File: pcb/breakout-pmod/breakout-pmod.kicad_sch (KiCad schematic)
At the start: 13 parts, among them J1 FX18-120P-0.8SV20

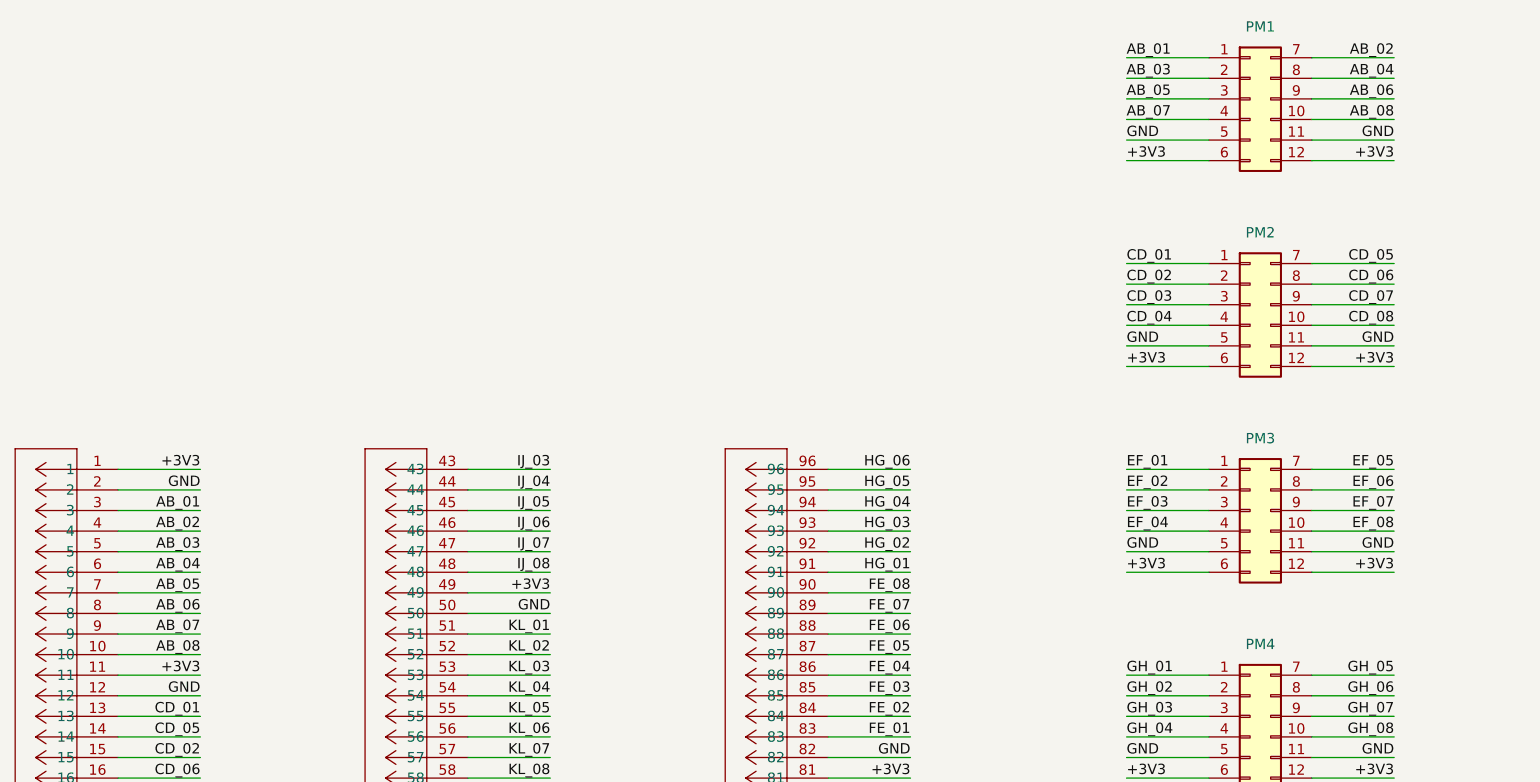
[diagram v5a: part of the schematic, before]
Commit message: [pmod] fix order of AB pmod
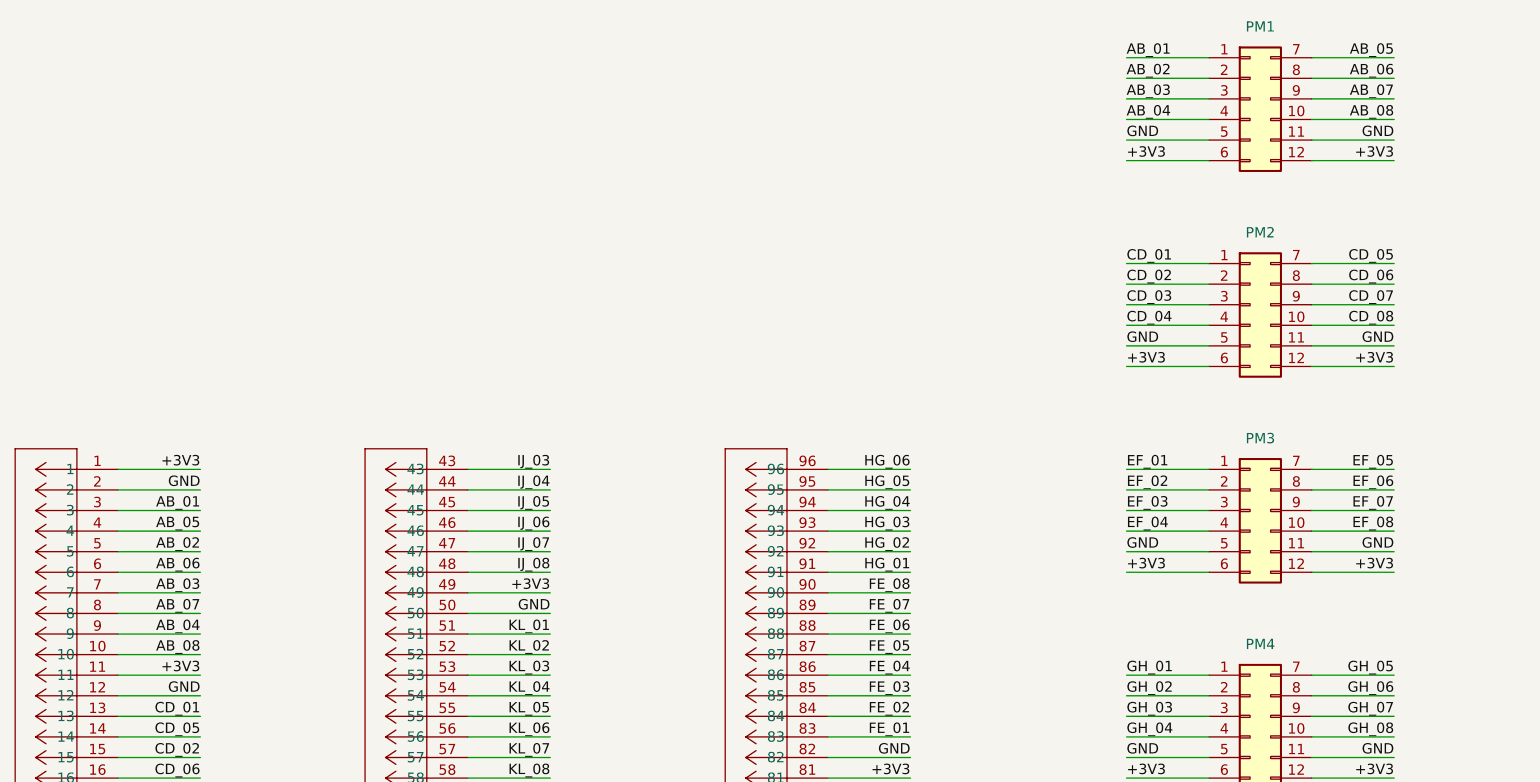
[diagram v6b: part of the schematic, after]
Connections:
- net AB_02: now also J1.5, PM1.2 (Pin_2); no longer J1.4, PM1.7 (Pin_7)
- net AB_03: now also J1.7, PM1.3 (Pin_3); no longer J1.5, PM1.2 (Pin_2)
- net AB_04: now also J1.9, PM1.4 (Pin_4); no longer J1.6, PM1.8 (Pin_8)
- net AB_05: now also J1.4, PM1.7 (Pin_7); no longer J1.7, PM1.3 (Pin_3)
- net AB_06: now also J1.6, PM1.8 (Pin_8); no longer J1.8, PM1.9 (Pin_9)
- net AB_07: now also J1.8, PM1.9 (Pin_9); no longer J1.9, PM1.4 (Pin_4)
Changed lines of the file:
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@@
 	)
 	(label "AB_07"
-		(at 50.8 110.49 180)
+		(at 50.8 107.95 180)
 		(fields_autoplaced yes)
 		(effects
@@
 	)
 	(label "AB_02"
-		(at 198.12 39.37 180)
-		(fields_autoplaced yes)
-		(effects
-			(font
-				(size 1.27 1.27)
-			)
-			(justify right bottom)
+		(at 165.1 41.91 0)
+		(fields_autoplaced yes)
+		(effects
+			(font
+				(size 1.27 1.27)
+			)
+			(justify left bottom)
 		)
 	)
@@
 	)
 	(label "AB_07"
-		(at 165.1 46.99 0)
-		(fields_autoplaced yes)
-		(effects
-			(font
-				(size 1.27 1.27)
-			)
-			(justify left bottom)
+		(at 198.12 44.45 180)
+		(fields_autoplaced yes)
+		(effects
+			(font
+				(size 1.27 1.27)
+			)
+			(justify right bottom)
 		)
 	)
@@
 	)
 	(label "AB_03"
-		(at 50.8 100.33 180)
+		(at 50.8 105.41 180)
 		(fields_autoplaced yes)
 		(effects
@@
 	)
 	(label "AB_04"
-		(at 50.8 102.87 180)
+		(at 50.8 110.49 180)
 		(fields_autoplaced yes)
 		(effects
@@
 	)
 	(label "AB_06"
-		(at 50.8 107.95 180)
+		(at 50.8 102.87 180)
 		(fields_autoplaced yes)
 		(effects
@@
 	)
 	(label "AB_04"
-		(at 198.12 41.91 180)
-		(fields_autoplaced yes)
-		(effects
-			(font
-				(size 1.27 1.27)
-			)
-			(justify right bottom)
+		(at 165.1 46.99 0)
+		(fields_autoplaced yes)
+		(effects
+			(font
+				(size 1.27 1.27)
+			)
+			(justify left bottom)
 		)
 	)
@@
 	)
 	(label "AB_02"
-		(at 50.8 97.79 180)
+		(at 50.8 100.33 180)
 		(fields_autoplaced yes)
 		(effects
@@
 	)
 	(label "AB_03"
-		(at 165.1 41.91 0)
+		(at 165.1 44.45 0)
 		(fields_autoplaced yes)
 		(effects
@@
 	)
 	(label "AB_06"
-		(at 198.12 44.45 180)
+		(at 198.12 41.91 180)
 		(fields_autoplaced yes)
 		(effects
@@
 	)
 	(label "AB_05"
-		(at 50.8 105.41 180)
+		(at 50.8 97.79 180)
 		(fields_autoplaced yes)
 		(effects
@@
 	)
 	(label "AB_05"
-		(at 165.1 44.45 0)
-		(fields_autoplaced yes)
-		(effects
-			(font
-				(size 1.27 1.27)
-			)
-			(justify left bottom)
-		)
-	)
+		(at 198.12 39.37 180)
+		(fields_autoplaced yes)
+		(effects
+			(font
+				(size 1.27 1.27)
+			)
+			(justify right bottom)
+		)
+	)

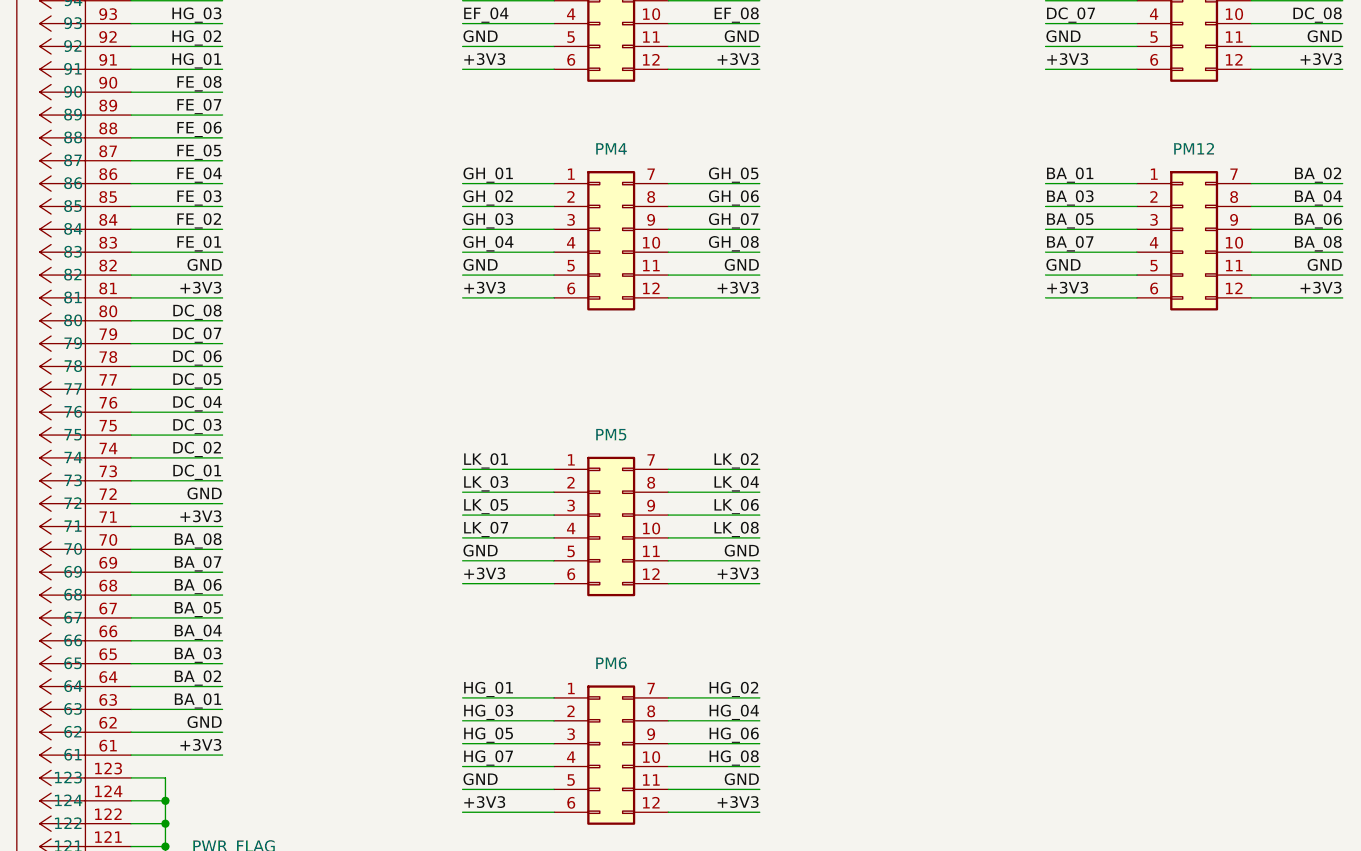
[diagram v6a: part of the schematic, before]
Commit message: [pmod] fix order of BA pmod
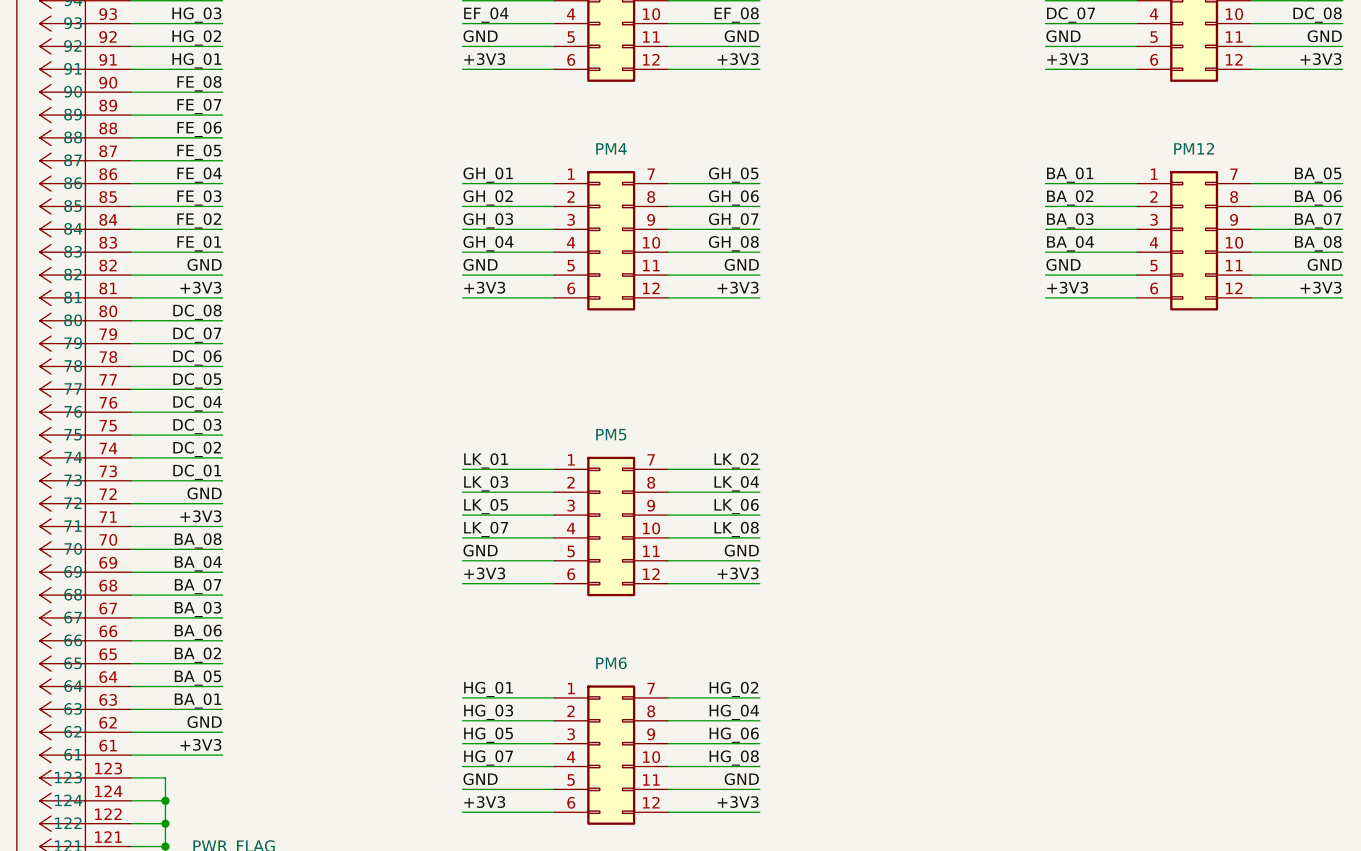
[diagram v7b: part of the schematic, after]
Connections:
- net BA_02: now also J1.65, PM12.2 (Pin_2); no longer J1.64, PM12.7 (Pin_7)
- net BA_03: now also J1.67, PM12.3 (Pin_3); no longer J1.65, PM12.2 (Pin_2)
- net BA_04: now also J1.69, PM12.4 (Pin_4); no longer J1.66, PM12.8 (Pin_8)
- net BA_05: now also J1.64, PM12.7 (Pin_7); no longer J1.67, PM12.3 (Pin_3)
- net BA_06: now also J1.66, PM12.8 (Pin_8); no longer J1.68, PM12.9 (Pin_9)
- net BA_07: now also J1.68, PM12.9 (Pin_9); no longer J1.69, PM12.4 (Pin_4)
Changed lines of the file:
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@@
 	)
 	(label "BA_03"
-		(at 138.43 168.91 180)
+		(at 138.43 163.83 180)
 		(fields_autoplaced yes)
 		(effects
@@
 	)
 	(label "BA_03"
-		(at 229.87 118.11 0)
+		(at 229.87 120.65 0)
 		(fields_autoplaced yes)
 		(effects
@@
 	)
 	(label "BA_05"
-		(at 229.87 120.65 0)
-		(fields_autoplaced yes)
-		(effects
-			(font
-				(size 1.27 1.27)
-			)
-			(justify left bottom)
+		(at 262.89 115.57 180)
+		(fields_autoplaced yes)
+		(effects
+			(font
+				(size 1.27 1.27)
+			)
+			(justify right bottom)
 		)
 	)
@@
 	)
 	(label "BA_02"
-		(at 138.43 171.45 180)
+		(at 138.43 168.91 180)
 		(fields_autoplaced yes)
 		(effects
@@
 	)
 	(label "BA_04"
-		(at 138.43 166.37 180)
+		(at 138.43 158.75 180)
 		(fields_autoplaced yes)
 		(effects
@@
 	)
 	(label "BA_06"
-		(at 262.89 120.65 180)
+		(at 262.89 118.11 180)
 		(fields_autoplaced yes)
 		(effects
@@
 	)
 	(label "BA_02"
-		(at 262.89 115.57 180)
-		(fields_autoplaced yes)
-		(effects
-			(font
-				(size 1.27 1.27)
-			)
-			(justify right bottom)
+		(at 229.87 118.11 0)
+		(fields_autoplaced yes)
+		(effects
+			(font
+				(size 1.27 1.27)
+			)
+			(justify left bottom)
 		)
 	)
@@
 	)
 	(label "BA_06"
-		(at 138.43 161.29 180)
+		(at 138.43 166.37 180)
 		(fields_autoplaced yes)
 		(effects
@@
 	)
 	(label "BA_05"
-		(at 138.43 163.83 180)
+		(at 138.43 171.45 180)
 		(fields_autoplaced yes)
 		(effects
@@
 	)
 	(label "BA_07"
-		(at 229.87 123.19 0)
-		(fields_autoplaced yes)
-		(effects
-			(font
-				(size 1.27 1.27)
-			)
-			(justify left bottom)
+		(at 262.89 120.65 180)
+		(fields_autoplaced yes)
+		(effects
+			(font
+				(size 1.27 1.27)
+			)
+			(justify right bottom)
 		)
 	)
@@
 	)
 	(label "BA_04"
-		(at 262.89 118.11 180)
-		(fields_autoplaced yes)
-		(effects
-			(font
-				(size 1.27 1.27)
-			)
-			(justify right bottom)
+		(at 229.87 123.19 0)
+		(fields_autoplaced yes)
+		(effects
+			(font
+				(size 1.27 1.27)
+			)
+			(justify left bottom)
 		)
 	)
@@
 	)
 	(label "BA_07"
-		(at 138.43 158.75 180)
-		(fields_autoplaced yes)
-		(effects
+		(at 138.43 161.29 180)
+		(fields_autoplaced yes)
+		(effects

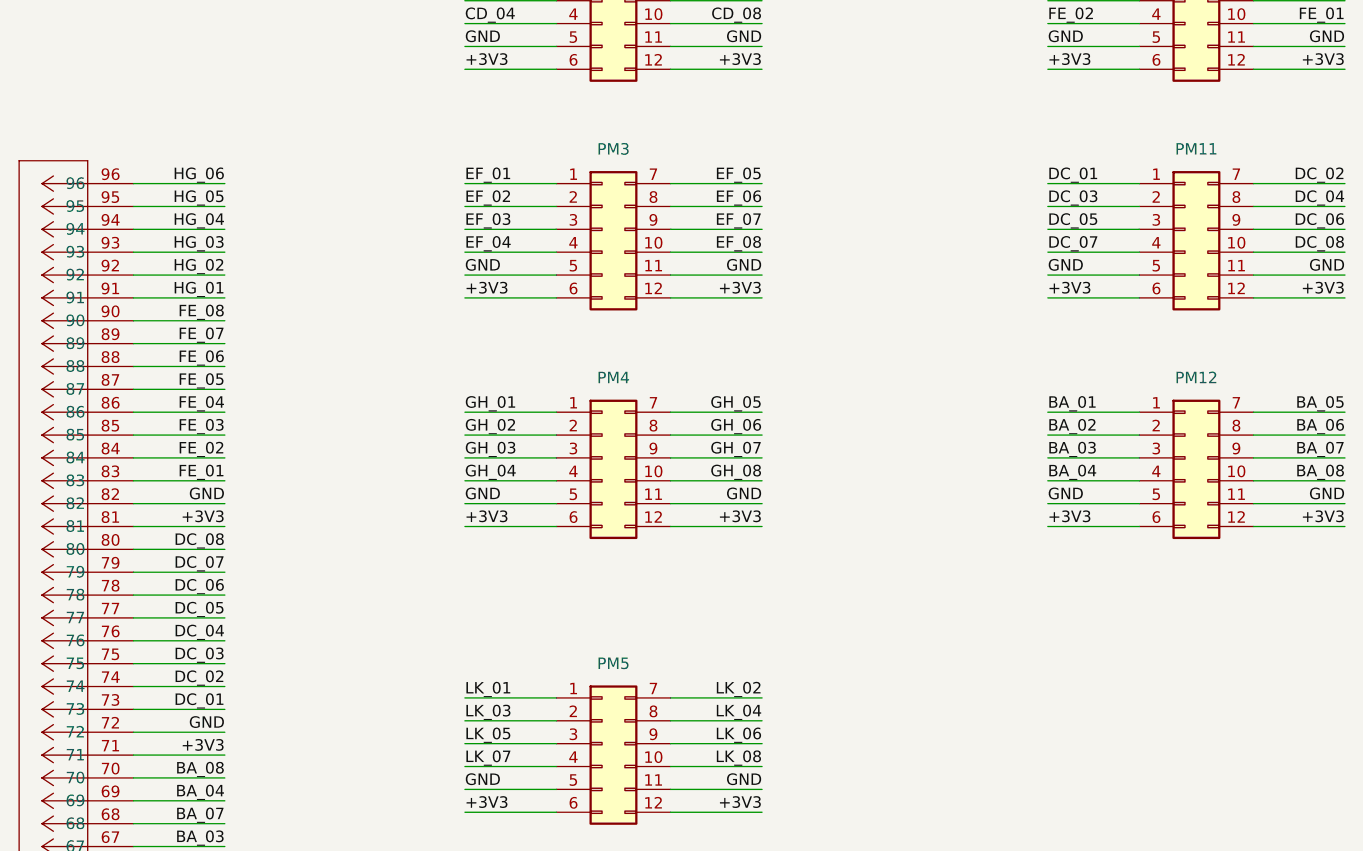
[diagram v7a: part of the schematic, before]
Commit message: [pmod] fix order of DC pmod
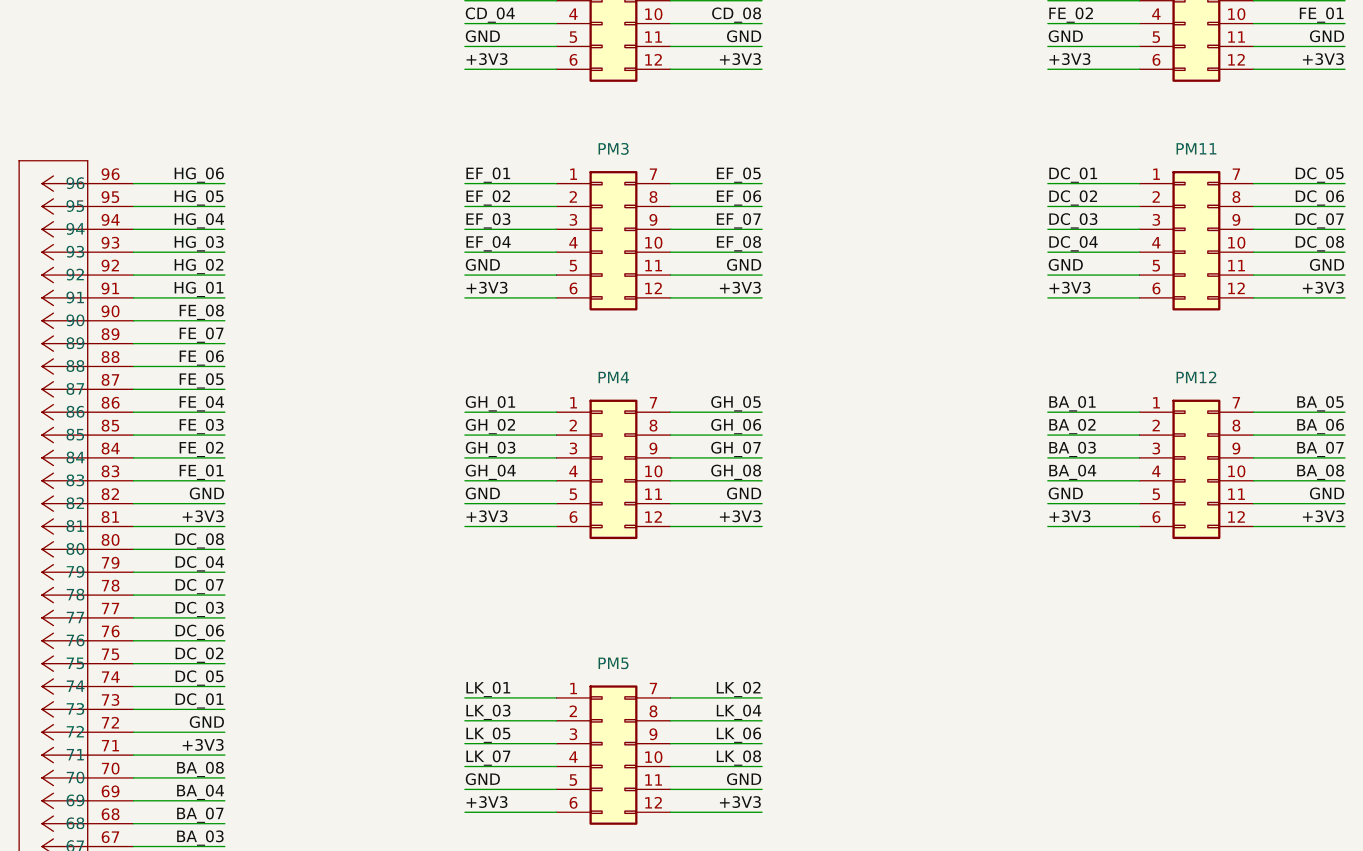
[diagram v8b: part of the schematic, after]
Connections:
- net DC_02: now also J1.75, PM11.2 (Pin_2); no longer J1.74, PM11.7 (Pin_7)
- net DC_03: now also J1.77, PM11.3 (Pin_3); no longer J1.75, PM11.2 (Pin_2)
- net DC_04: now also J1.79, PM11.4 (Pin_4); no longer J1.76, PM11.8 (Pin_8)
- net DC_05: now also J1.74, PM11.7 (Pin_7); no longer J1.77, PM11.3 (Pin_3)
- net DC_06: now also J1.76, PM11.8 (Pin_8); no longer J1.78, PM11.9 (Pin_9)
- net DC_07: now also J1.78, PM11.9 (Pin_9); no longer J1.79, PM11.4 (Pin_4)
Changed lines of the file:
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@@
 	)
 	(label "DC_07"
-		(at 138.43 133.35 180)
+		(at 138.43 135.89 180)
 		(fields_autoplaced yes)
 		(effects
@@
 	)
 	(label "DC_04"
-		(at 138.43 140.97 180)
+		(at 138.43 133.35 180)
 		(fields_autoplaced yes)
 		(effects
@@
 	)
 	(label "DC_03"
-		(at 229.87 92.71 0)
+		(at 229.87 95.25 0)
 		(fields_autoplaced yes)
 		(effects
@@
 	)
 	(label "DC_06"
-		(at 138.43 135.89 180)
+		(at 138.43 140.97 180)
 		(fields_autoplaced yes)
 		(effects
@@
 	)
 	(label "DC_02"
-		(at 262.89 90.17 180)
-		(fields_autoplaced yes)
-		(effects
-			(font
-				(size 1.27 1.27)
-			)
-			(justify right bottom)
+		(at 229.87 92.71 0)
+		(fields_autoplaced yes)
+		(effects
+			(font
+				(size 1.27 1.27)
+			)
+			(justify left bottom)
 		)
 	)
@@
 	)
 	(label "DC_05"
-		(at 138.43 138.43 180)
+		(at 138.43 146.05 180)
 		(fields_autoplaced yes)
 		(effects
@@
 	)
 	(label "DC_07"
-		(at 229.87 97.79 0)
-		(fields_autoplaced yes)
-		(effects
-			(font
-				(size 1.27 1.27)
-			)
-			(justify left bottom)
+		(at 262.89 95.25 180)
+		(fields_autoplaced yes)
+		(effects
+			(font
+				(size 1.27 1.27)
+			)
+			(justify right bottom)
 		)
 	)
@@
 	)
 	(label "DC_03"
-		(at 138.43 143.51 180)
+		(at 138.43 138.43 180)
 		(fields_autoplaced yes)
 		(effects
@@
 	)
 	(label "DC_05"
-		(at 229.87 95.25 0)
-		(fields_autoplaced yes)
-		(effects
-			(font
-				(size 1.27 1.27)
-			)
-			(justify left bottom)
+		(at 262.89 90.17 180)
+		(fields_autoplaced yes)
+		(effects
+			(font
+				(size 1.27 1.27)
+			)
+			(justify right bottom)
 		)
 	)
@@
 	)
 	(label "DC_02"
-		(at 138.43 146.05 180)
+		(at 138.43 143.51 180)
 		(fields_autoplaced yes)
 		(effects
@@
 	)
 	(label "DC_06"
-		(at 262.89 95.25 180)
+		(at 262.89 92.71 180)
 		(fields_autoplaced yes)
 		(effects
@@
 	)
 	(label "DC_04"
-		(at 262.89 92.71 180)
-		(fields_autoplaced yes)
-		(effects
-			(font
-				(size 1.27 1.27)
-			)
-			(justify right bottom)
-		)
-	)
+		(at 229.87 97.79 0)
+		(fields_autoplaced yes)
+		(effects
+			(font
+				(size 1.27 1.27)
+			)
+			(justify left bottom)
+		)
+	)
